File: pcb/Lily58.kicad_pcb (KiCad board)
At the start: 2 copper layers, 142.5 x 106.3 mm, 123 parts, among them J1 LED, J2 4PIN, P1 i2c_pin, P2 i2c_pin, P3 ICSP, P4 OLED, SW1 SW_PUSH, SW10 SW_PUSH, SW11 SW_PUSH, SW12 SW_PUSH, SW13 SW_PUSH, SW14 SW_PUSH, SW15 SW_PUSH, SW16 SW_PUSH, SW17 SW_PUSH, SW18 SW_PUSH, SW19 SW_PUSH, SW2 SW_PUSH, SW20 SW_PUSH, SW21 SW_PUSH, SW22 SW_PUSH, SW23 SW_PUSH, SW24 SW_PUSH, SW25 SW_PUSH, SW26 SW_PUSH, SW27 SW_PUSH, SW28 SW_PUSH, SW29 SW_PUSH, SW3 SW_PUSH, SW4 SW_PUSH, SW5 SW_PUSH, SW6 SW_PUSH, SW7 SW_PUSH, SW8 SW_PUSH, SW9 SW_PUSH, U1 ProMicro

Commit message: add LED for BLE Micro Pro indicator
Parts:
- removed P3: ICSP, Lily58-footprint:ICSP
- added D31: S-562T, Diode_SMD:D_1206_3216Metric_Pad1.42x1.75mm_HandSolder, B.Cu at (88.7, 78.8)
- added D31: S-562T, Diode_SMD:D_1206_3216Metric_Pad1.42x1.75mm_HandSolder, F.Cu at (88.7, 78.8)
- added LED1: SMLE13BC8TT86, Diode_SMD:D_0603_1608Metric_Pad1.05x0.95mm_HandSolder, B.Cu at (85.0, 79.5)
- added LED1: SMLE13BC8TT86, Diode_SMD:D_0603_1608Metric_Pad1.05x0.95mm_HandSolder, F.Cu at (85.0, 79.5)
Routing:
- net Net-(LED1-Pad2): track 17.0 -> 42.2 mm, vias 1 -> 2
- net col3: track 300.9 -> 283.2 mm
- net col2: track 314.4 -> 297.4 mm, vias 1 -> 0
- net VCC: track 1030.4 -> 1013.7 mm
- net col4: track 291.3 -> 283.2 mm
- net RESET: track 57.5 -> 50.3 mm
- net GND: track 1068.1 -> 1073.3 mm
- net Net-(D31-Pad2): track 0.00 -> 3.74 mm, vias 0 -> 2
- net DATA: track 59.0 -> 57.1 mm
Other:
- outline, holes or cut-outs redrawn
- board text added: "https://github.com/deIucq/Lily58-Glow"
- board text removed: "Lily58 × qtkb"

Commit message: change pinsocket 4pin -> 6pin
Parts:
- removed the D31 at (88.7, 78.8) (x2)
- removed the LED1 at (85.0, 79.5) (x2)
- removed P4: OLED, Lily58-footprint:MY_SIL-4
- added D31: S-562T, Lily58-footprint:D_1206_3216Metric_Pad1.42x1.75mm_HandSolder, F.Cu at (88.7, 78.8)
- added J3: Conn_01x06_Female, Lily58-footprint:OLED_4Pin, F.Cu at (104.2, 74.6)
- added LED1: SMLE13BC8TT86, Lily58-footprint:LED_0603_1608Metric_Pad1.05x0.95mm_HandSolder, F.Cu at (85.0, 79.5)
- moved G*** 1.85 mm to (97.0, 83.0) (x2)
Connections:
- U1 pad 19: Net-(U1-Pad19) -> A2
- U1 pad 20: Net-(U1-Pad20) -> A3
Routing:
- net A2: track 0.00 -> 42.4 mm, vias 0 -> 1
- net A3: track 0.00 -> 37.3 mm, vias 0 -> 1
- net Net-(U1-Pad20): track 14.4 -> 0.00 mm
- net Net-(U1-Pad19): track 14.4 -> 0.00 mm
- net GND: track 1073.3 -> 1066.7 mm
- net VCC: track 1013.7 -> 1018.0 mm, vias 43 -> 44
- net DATA: track 57.1 -> 59.0 mm
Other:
- board text added: "LED1"

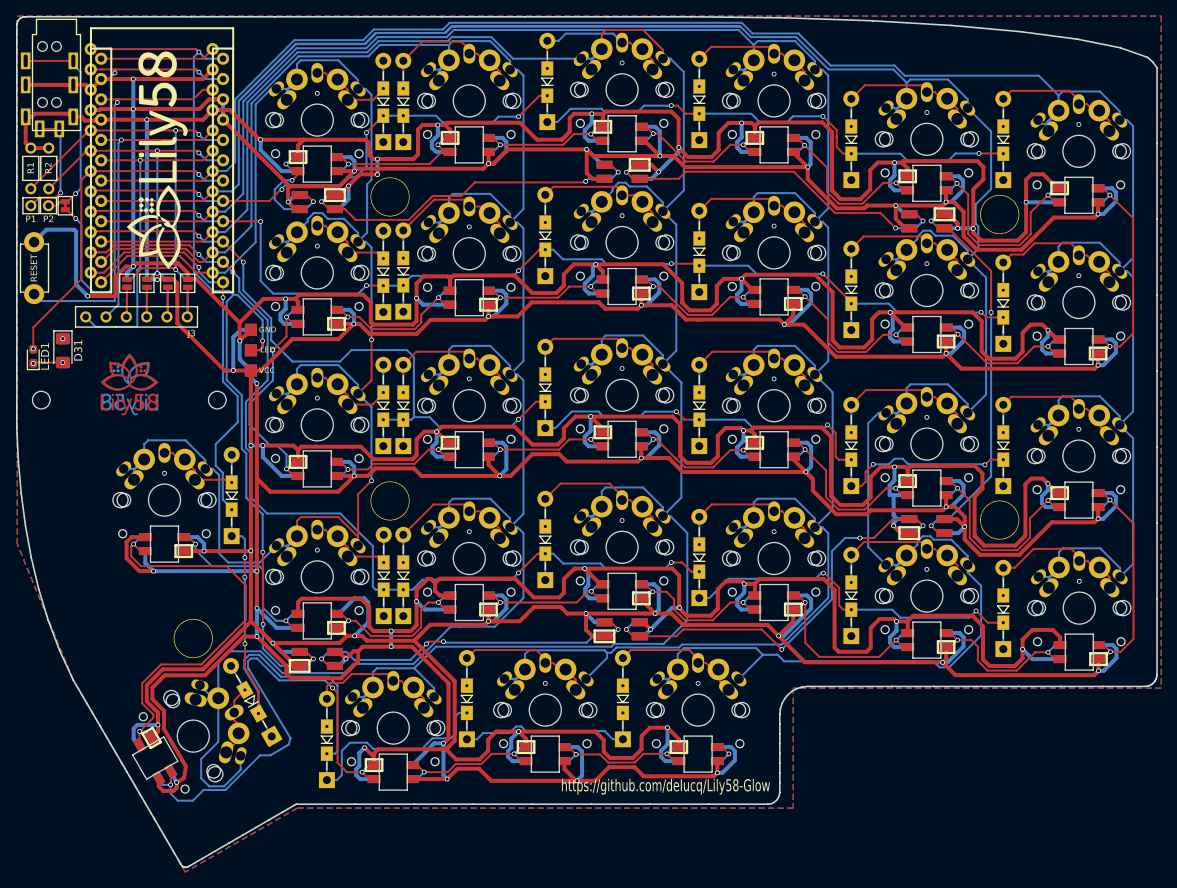
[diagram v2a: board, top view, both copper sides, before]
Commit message: changed LED pad for SK6812MINI-E
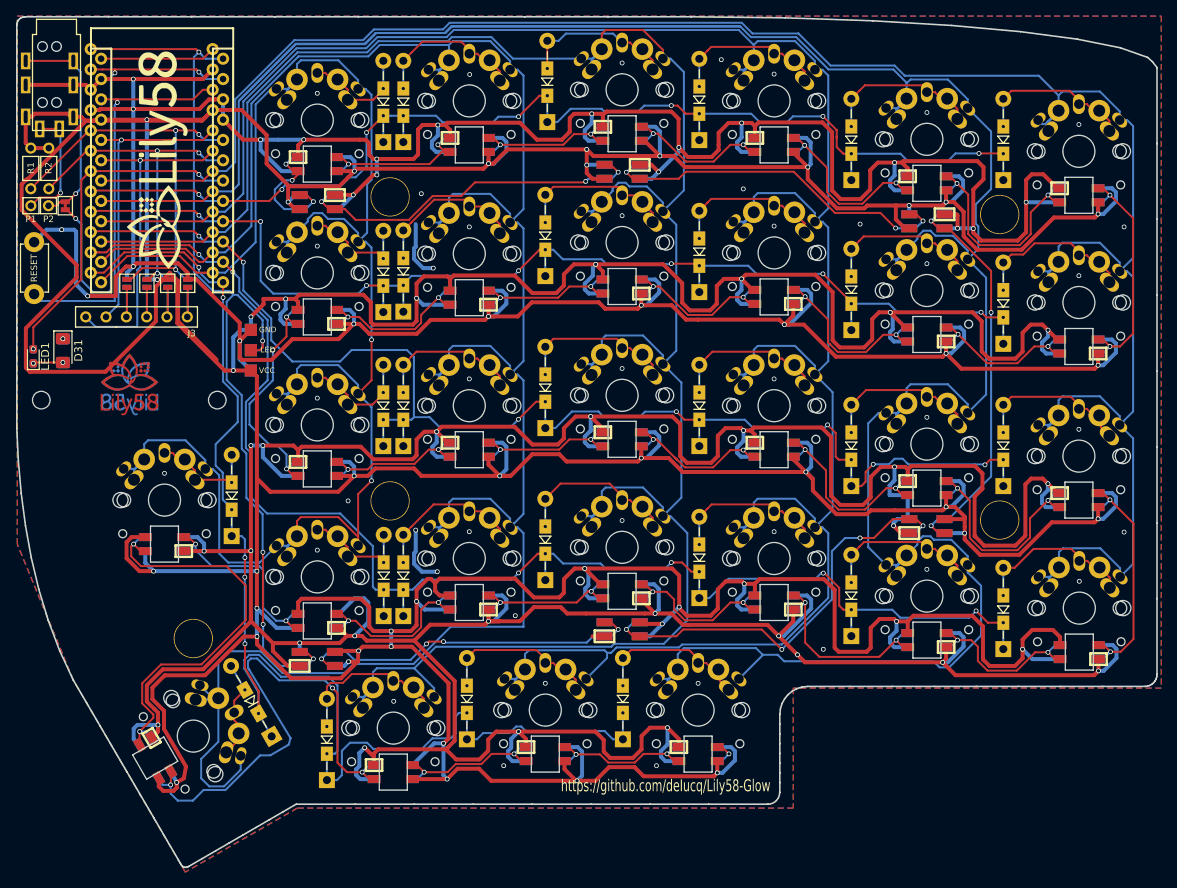
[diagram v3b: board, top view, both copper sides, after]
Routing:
- net VCC: track 1018.0 -> 1128.7 mm, vias 44 -> 47
- net GND: track 1066.7 -> 1057.8 mm, vias 74 -> 91
- net col4: track 283.2 -> 285.3 mm

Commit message: change pad and delete underglow
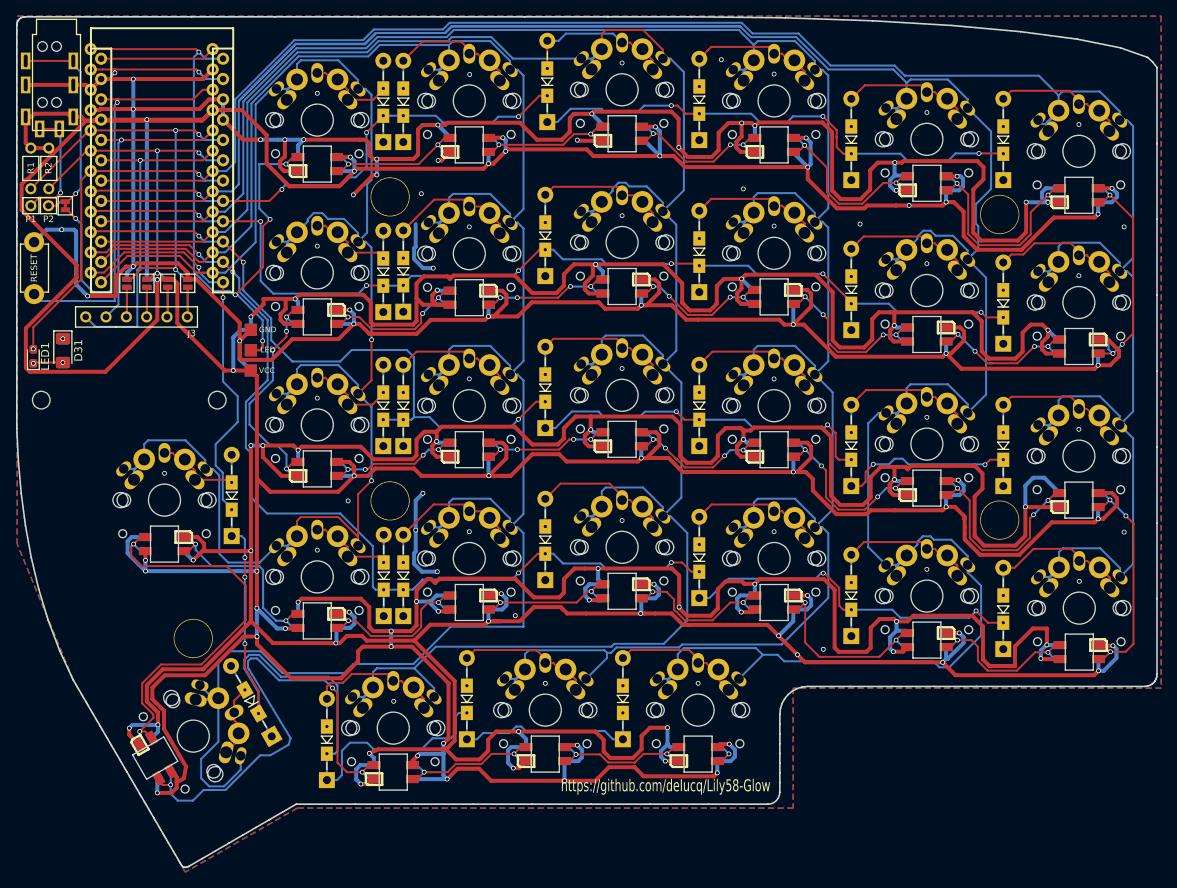
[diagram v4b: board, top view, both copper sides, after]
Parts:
- removed G*** (x2): LOGO, Lily58-footprint:lily58_logo_2
- removed G*** (x2): LOGO, Lily58-footprint:lily58_logo_3
- removed L30, L31, L32, L33, L34, L35: SK6812mini, Lily58-footprint:SK6812MINI_underglow_rev
- moved SW10 0.05 mm to (177.6, 66.7)
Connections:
- L1 pad 3: Net-(L1-Pad3) -> LED
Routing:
- net Net-(L34-Pad1): track 53.6 -> 0.00 mm, vias 4 -> 0
- net Net-(L32-Pad3): track 49.9 -> 0.00 mm, vias 3 -> 0
- net Net-(L31-Pad3): track 45.2 -> 0.00 mm, vias 3 -> 0
- net Net-(L30-Pad3): track 44.6 -> 0.00 mm, vias 3 -> 0
- net Net-(L33-Pad1): track 43.7 -> 0.00 mm, vias 4 -> 0
- net LED: track 121.3 -> 90.4 mm
- net VCC: track 1128.7 -> 1098.2 mm, vias 47 -> 59
- net GND: track 1057.8 -> 1034.3 mm, vias 91 -> 103
- net Net-(L1-Pad3): track 16.9 -> 0.00 mm, vias 3 -> 0
- net Net-(L2-Pad1): track 20.1 -> 16.7 mm
- net Net-(L19-Pad1): track 25.9 -> 23.4 mm
- net Net-(L14-Pad1): track 19.3 -> 16.8 mm, vias 2 -> 4
- net Net-(L27-Pad1): track 19.6 -> 17.1 mm
- net Net-(L15-Pad1): track 21.3 -> 18.9 mm, vias 2 -> 4
- net Net-(L28-Pad1): track 19.6 -> 17.2 mm
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
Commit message: add pinheader and logo
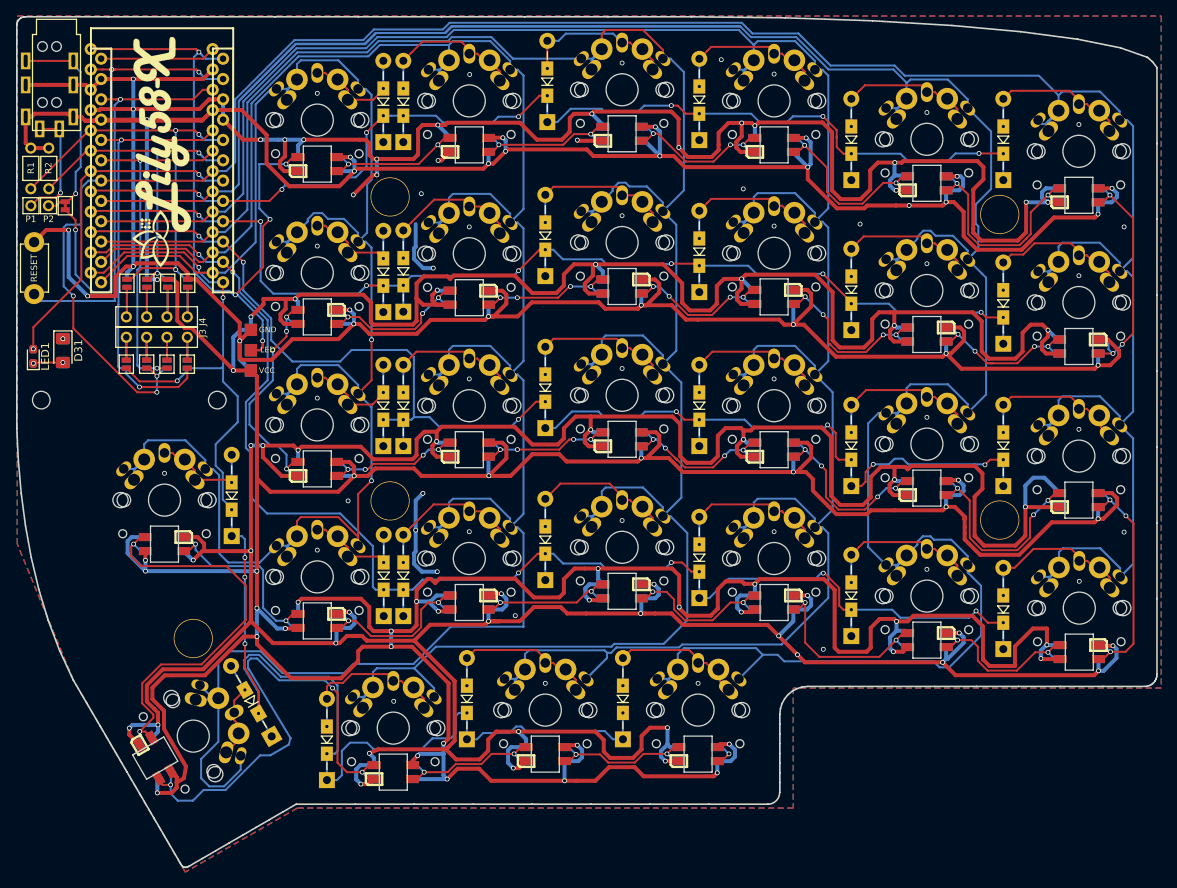
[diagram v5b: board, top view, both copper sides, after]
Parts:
- added G***: LOGO, Lily58-footprint:lily58_x_logo, B.Cu at (101.1, 56.2)
- added G***: LOGO, Lily58-footprint:lily58_x_logo, F.Cu at (101.1, 51.8)
- added J4: Conn_01x06_Female, Lily58-footprint:OLED_4Pin, F.Cu at (104.2, 77.1)
- added JP10: Jumper_NO_Small, Lily58-footprint:Jumper, B.Cu at (101.7, 80.5)
- added JP11: Jumper_NO_Small, Lily58-footprint:Jumper, B.Cu at (99.2, 80.5)
- added JP12: Jumper_NO_Small, Lily58-footprint:Jumper, B.Cu at (96.6, 80.5)
- added JP13: Jumper_NO_Small, Lily58-footprint:Jumper, F.Cu at (104.2, 80.5)
- added JP14: Jumper_NO_Small, Lily58-footprint:Jumper, F.Cu at (101.7, 80.5)
- added JP15: Jumper_NO_Small, Lily58-footprint:Jumper, F.Cu at (99.2, 80.5)
- added JP16: Jumper_NO_Small, Lily58-footprint:Jumper, F.Cu at (96.6, 80.5)
- added JP9: Jumper_NO_Small, Lily58-footprint:Jumper, B.Cu at (104.2, 80.5)
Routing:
- net VCC: track 1098.2 -> 1034.0 mm
- net col0: track 270.9 -> 312.9 mm, vias 0 -> 3
- net A3: track 37.3 -> 54.8 mm, vias 1 -> 2
- net row4: track 167.1 -> 180.8 mm, vias 5 -> 6
- net Net-(J4-Pad1): track 0.00 -> 5.95 mm
- net Net-(J4-Pad4): track 0.00 -> 5.74 mm
- net Net-(J4-Pad3): track 0.00 -> 5.74 mm
- net Net-(J4-Pad2): track 0.00 -> 5.74 mm
- net A2: track 42.4 -> 44.1 mm, vias 1 -> 2
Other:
- board text removed: "Glow"
- board text removed: "https://github.com/deIucq/Lily58-Glow"

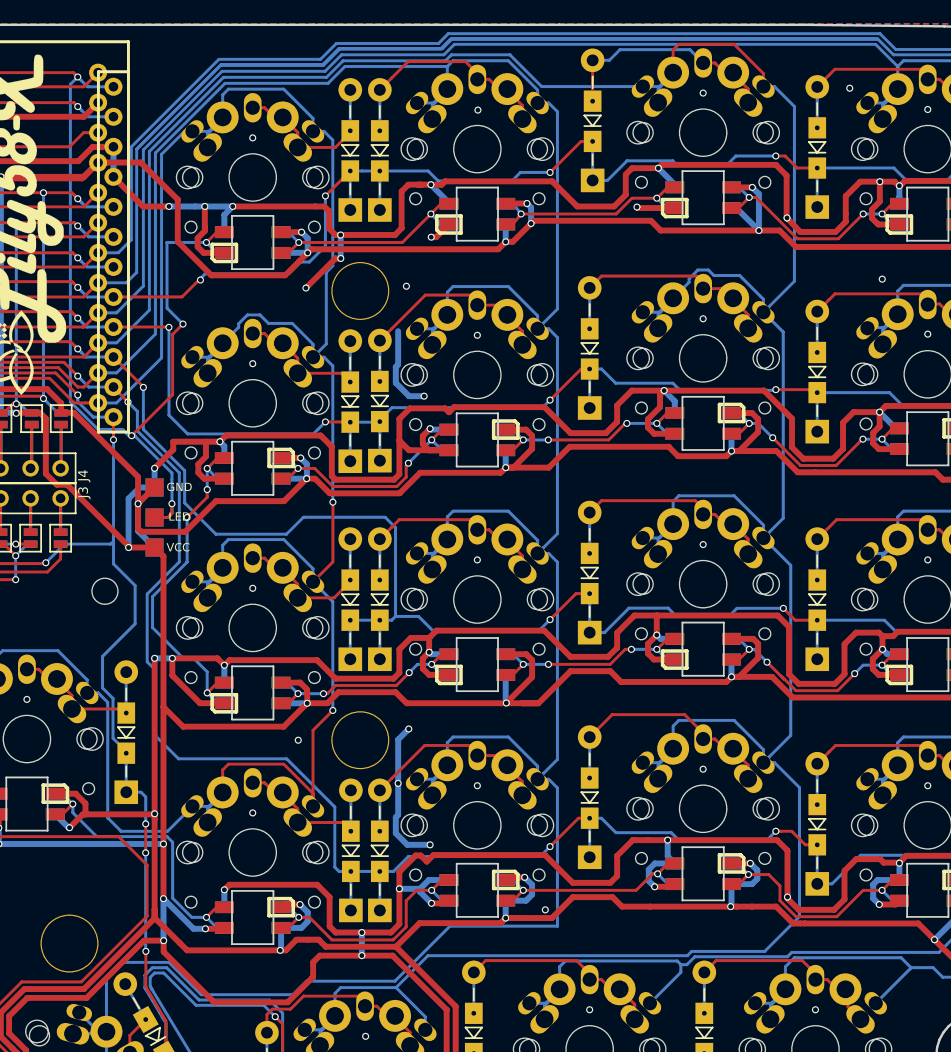
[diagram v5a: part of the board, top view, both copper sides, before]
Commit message: add via
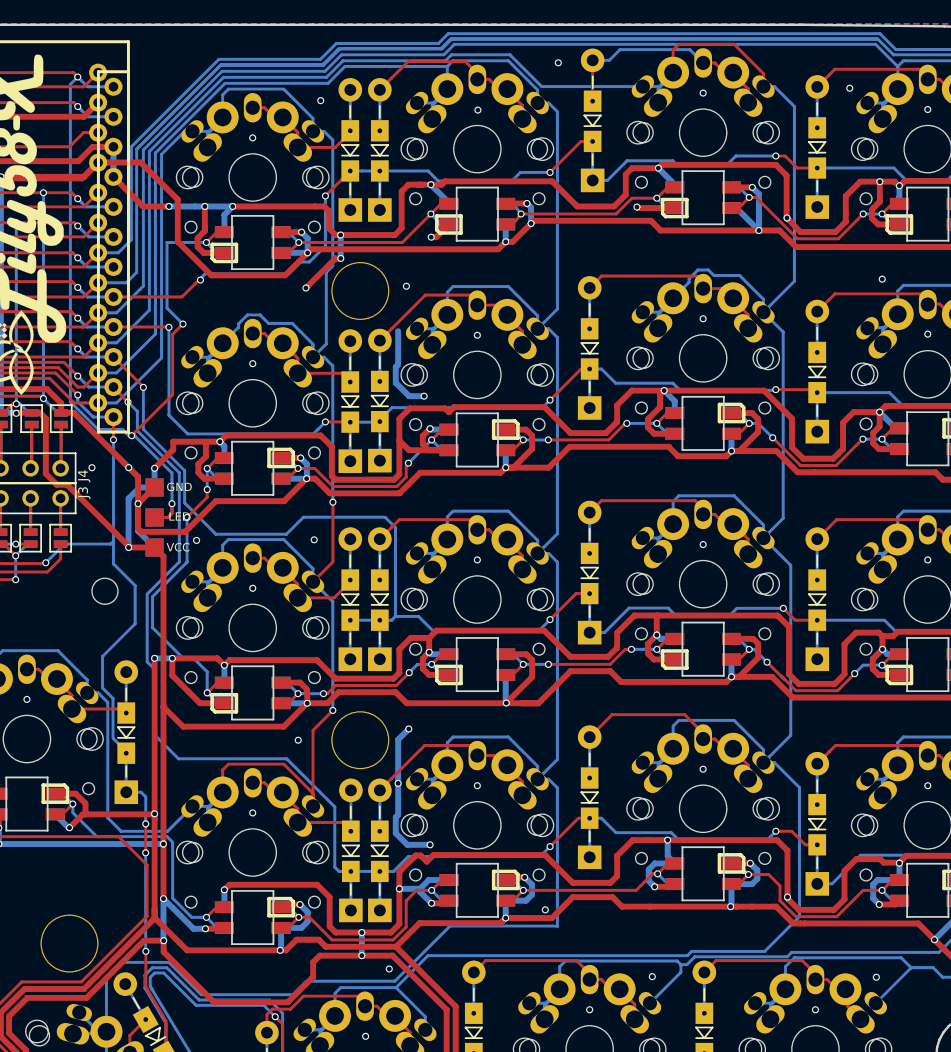
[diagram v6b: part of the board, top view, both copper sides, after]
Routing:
- net GND: vias 103 -> 112

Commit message: brush up PCB
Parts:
- removed J1: LED, Lily58-footprint:StripLED
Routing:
- net LED: track 90.4 -> 37.5 mm, vias 5 -> 3
- net GND: track 1033.8 -> 1028.0 mm, vias 112 -> 166
- net col0: track 312.9 -> 316.7 mm
- net col1: track 382.1 -> 385.8 mm
- net VCC: track 1034.0 -> 1031.0 mm, vias 59 -> 55
- net col2: track 297.4 -> 300.2 mm
- net col3: track 283.2 -> 285.7 mm
- net row2: track 167.2 -> 164.8 mm
- net col5: track 215.5 -> 216.7 mm
- net Net-(L1-Pad1): track 18.8 -> 17.7 mm
- net Net-(L12-Pad3): track 30.2 -> 29.2 mm
- net Net-(L25-Pad1): track 51.9 -> 51.4 mm
- net Net-(L26-Pad1): track 62.9 -> 63.4 mm
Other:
- board text added: "Lily58-"
- board text added: "χ"
- board text removed: "GND"
- board text removed: "LED"
- board text removed: "VCC"
